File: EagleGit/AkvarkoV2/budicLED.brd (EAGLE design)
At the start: 114.3 x 160 mm, 59 parts, among them IC1 7805TV, Q1 BD243C, Q2 BD243C, Q3 BD243C, Q4 BD243C, T1 2N5551, T2 2N5551, T3 2N5551, T4 2N5551, U1 ARDUINOR3-DIMENSION, X1 SMKDSP_1,5/2, X2 SMKDSP_1,5/8, X3 SMKDSP_1,5/3

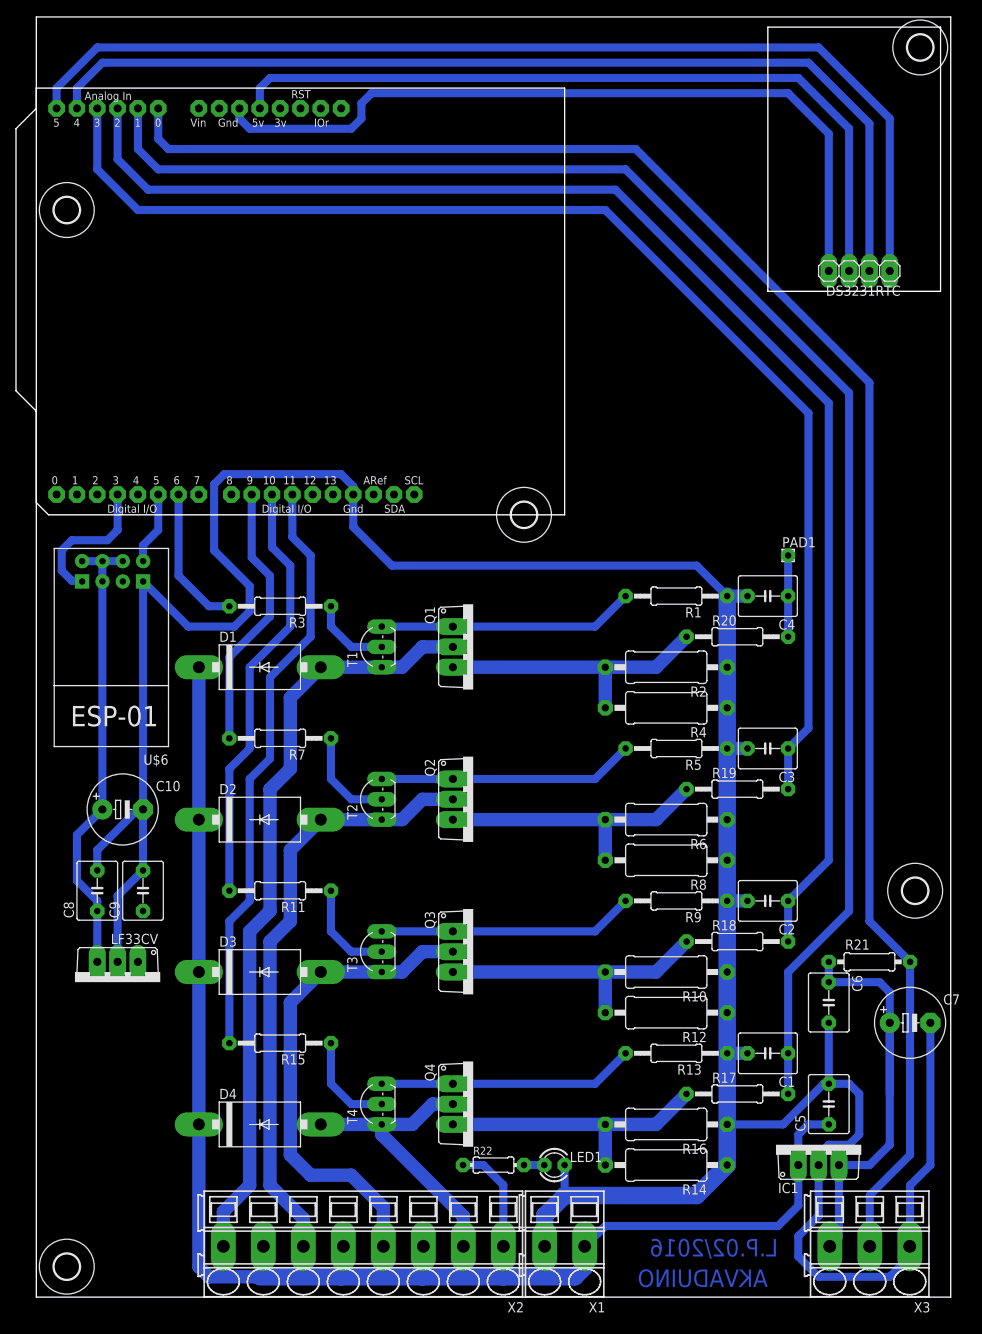
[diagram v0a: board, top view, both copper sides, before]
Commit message: Akvarko: - zakladni navrh DPS a rozmisteni soucastek.
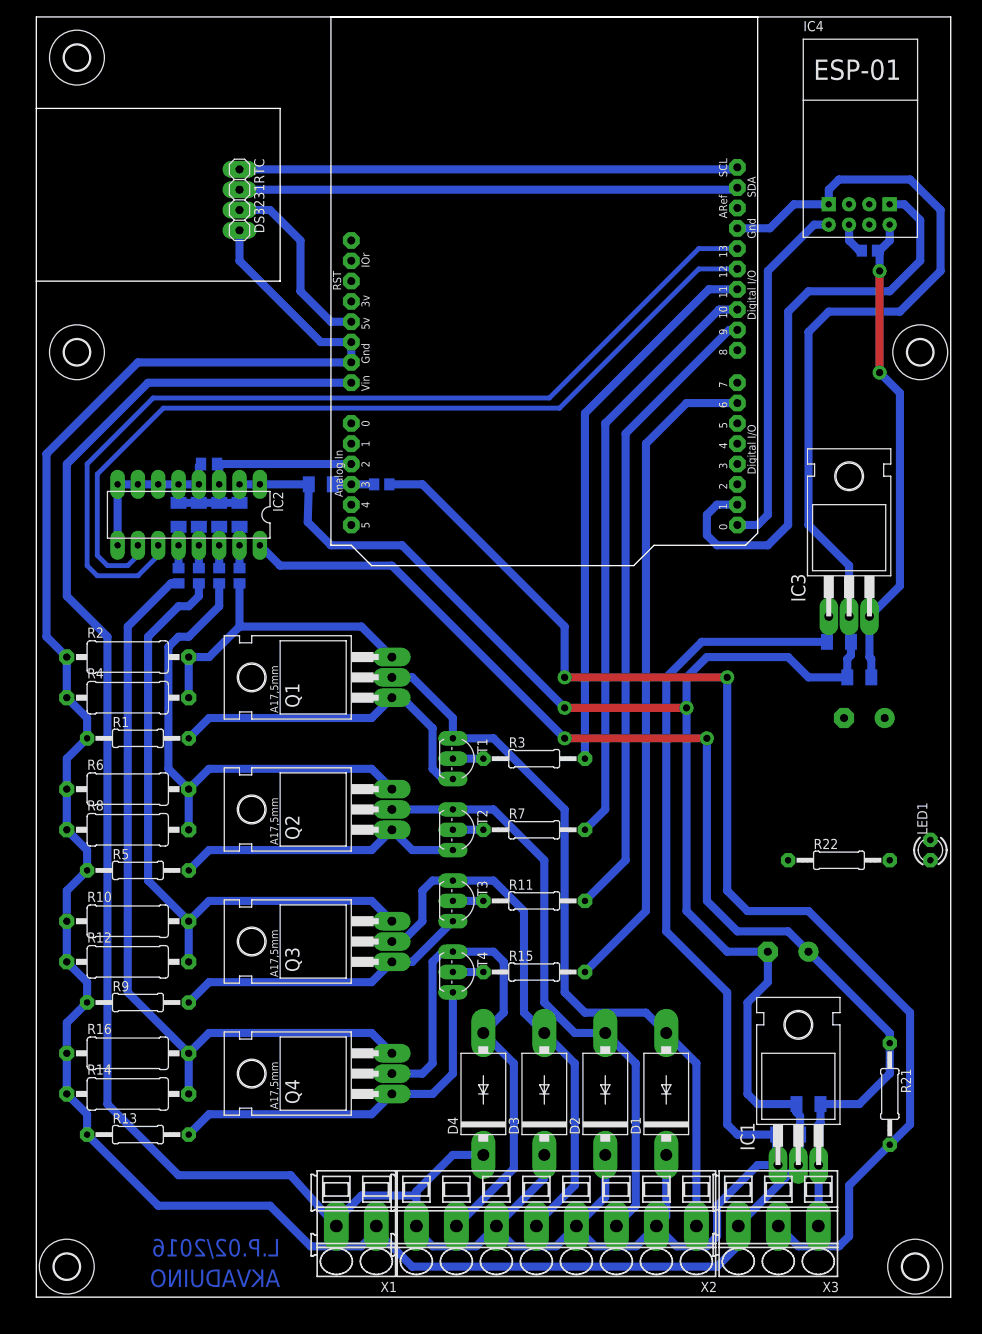
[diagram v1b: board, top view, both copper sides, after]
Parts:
- removed LF33CV: 7805TV, linear:TO220V
- removed PAD1: (no value), wirepad:1,6/0,8
- removed U$6: ESP01, esp8266modules:ESP01
- added C11: 330n, rcl:C0805K
- added C12: 330n, rcl:C1206K
- added IC2: 4051N, 40xx:DIL16
- added IC3: LF33CV, linear:TO220H
- added IC4: ESP01, esp8266modules:ESP01
- added R23, R24: 4k7, rcl:R0805
- C1, C2, C3, C4, C5, C6, C8, C9: device rcl:C050-050X075 -> rcl:C1206K
- C10, C7: device resistor:E5-8,5 -> resistor:E5-10,5
- IC1: value 7805TV -> 7805T; device linear:TO220V -> linear:TO220H
- Q1, Q2, Q3, Q4: device transistor:TO220V -> transistor:TO220
- R17, R18, R19, R20: device rcl:0207/12 -> rcl:R0805
- R21: device rcl:0207/10 -> rcl:0207/12
- R22: device rcl:0204/7 -> rcl:0207/12
- moved U$4 112.1 mm to (5.08, 118.1)
- moved C8 98.9 mm to (102.9, 77.5), flipped to the bottom, turned to 0 degrees
- moved C1 94.3 mm to (25.4, 97.8), flipped to the bottom, turned to 90 degrees
- moved C10 93.4 mm to (103.5, 72.4), flipped to the bottom
- moved C9 92.4 mm to (100.3, 81.9), flipped to the bottom, turned to 180 degrees
- moved R17 89.8 mm to (25.4, 90.2), flipped to the bottom, turned to 90 degrees
- moved C2 83.9 mm to (22.9, 97.8), flipped to the bottom, turned to 90 degrees
- moved R18 79.3 mm to (22.9, 90.2), flipped to the bottom, turned to 90 degrees
- moved DS3231RTC 78.0 mm to (25.4, 137.2), turned to 270 degrees
- moved C3 76.9 mm to (20.3, 97.8), flipped to the bottom, turned to 90 degrees
- moved C4 74.4 mm to (17.8, 97.8), flipped to the bottom, turned to 90 degrees
- moved D1 73.7 mm to (78.7, 25.4), turned to 90 degrees
- moved R19 72.4 mm to (20.3, 90.2), flipped to the bottom, turned to 90 degrees
- moved R20 70.3 mm to (17.8, 90.2), flipped to the bottom, turned to 90 degrees
- moved R1 69.6 mm to (12.7, 69.8), turned to 0 degrees
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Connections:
- removed net +5V: C9.1, DS3231RTC.3, LF33CV.1, U1.5V
- removed net GND1: U1.GND1
- removed net N$16: R15.2, U1.D11
- removed net N$26: DS3231RTC.4, U1.GND2
- removed net VIN: U1.VIN
- new net N$29: C1.1, IC2.15, R17.2
- new net N$30: C2.1, IC2.14, R18.2
- new net N$31: C3.1, IC2.13, R19.2
- new net N$32: IC2.10, U1.D12
- new net N$33: C4.1, IC2.12, R20.2
- new net N$34: R3.2, U1.D11
- new net N$35: R15.2, U1.D6
- net +12V: now also C9.1, IC3.1, U1.VIN, X1.2, X2.2, X2.4, X2.6, X2.8; no longer X1.1, X2.1, X2.3, X2.5, X2.7
- net +3V3: now also IC3.3, IC4.VCC, R23.1; no longer LF33CV.3, U$6.CH_PD, U$6.VCC
- net GND: now also C11.2, C12.2, DS3231RTC.4, IC2.1, IC2.2, IC2.4, IC2.5, IC2.6, IC2.7, IC2.8, IC2.9, IC3.2, IC4.GND, U1.GND1, U1.GND2, X1.1, X3.3; no longer LF33CV.2, U$6.GND, X1.2, X3.1
- net N$10: now also R21.2, R24.1, X3.2; no longer R3.2, U1.D6
- net N$13: now also U1.SCL; no longer U1.A5
- net N$15: now also U1.D9; no longer U1.D10
- net N$17: now also IC4.CH_PD, R23.2; no longer C4.1, PAD1.1, R20.2
- net N$18: now also C11.1, IC2.3; no longer C2.1, R18.2
- net N$19: now also DS3231RTC.3, U1.5V; no longer C3.1, R19.2, U1.A3
- net N$2: now also X2.1; no longer X2.8
- net N$20: now also IC2.11, U1.D13; no longer C1.1, R17.2, U1.A1
- net N$21: now also C12.1, R24.2, U1.A3; no longer R21.2, U1.A0, X3.2
- net N$22: now also U1.D10; no longer U1.D9
- net N$23: now also IC2.16, X3.1; no longer X3.3
- net N$24: now also U1.SDA; no longer U1.A4
- net N$25: now also IC4.TX, U1.D0; no longer U$6.TX, U1.D5
- net N$28: now also IC4.RX, U1.D1; no longer U$6.RX, U1.D3
- net N$4: now also X2.3; no longer X2.6
- net N$5: now also X2.5; no longer X2.4
- net N$7: now also X2.7; no longer X2.2
- net SENS1: now also R20.1; no longer R17.1
- net SENS2: now also R19.1; no longer R18.1
- net SENS3: now also R18.1; no longer R19.1
- net SENS4: now also R17.1; no longer R20.1
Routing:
- net N$21: track 217.5 -> 5.17 mm
- net GND: track 379.8 -> 570.7 mm, vias 0 -> 2
- net +12V: track 199.5 -> 369.2 mm
- net N$18: track 177.3 -> 19.4 mm
- net N$10: track 18.1 -> 153.3 mm, vias 0 -> 2
- net N$19: track 157.2 -> 23.5 mm
- net N$32: track 0.00 -> 108.2 mm
- net N$26: track 97.7 -> 0.00 mm
- net +5V: track 97.1 -> 0.00 mm
- net N$23: track 56.7 -> 146.6 mm, vias 0 -> 2
- net N$35: track 0.00 -> 82.7 mm
- net N$20: track 197.4 -> 116.9 mm
- net N$16: track 73.7 -> 0.00 mm
- net N$13: track 131.5 -> 62.3 mm
- net N$34: track 0.00 -> 68.6 mm
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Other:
- outline, holes or cut-outs redrawn

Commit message: Akvarko2: - navržené DPS. x bylo by vhodné doplnit filtrační kondenzátory k napájecím vstupům.
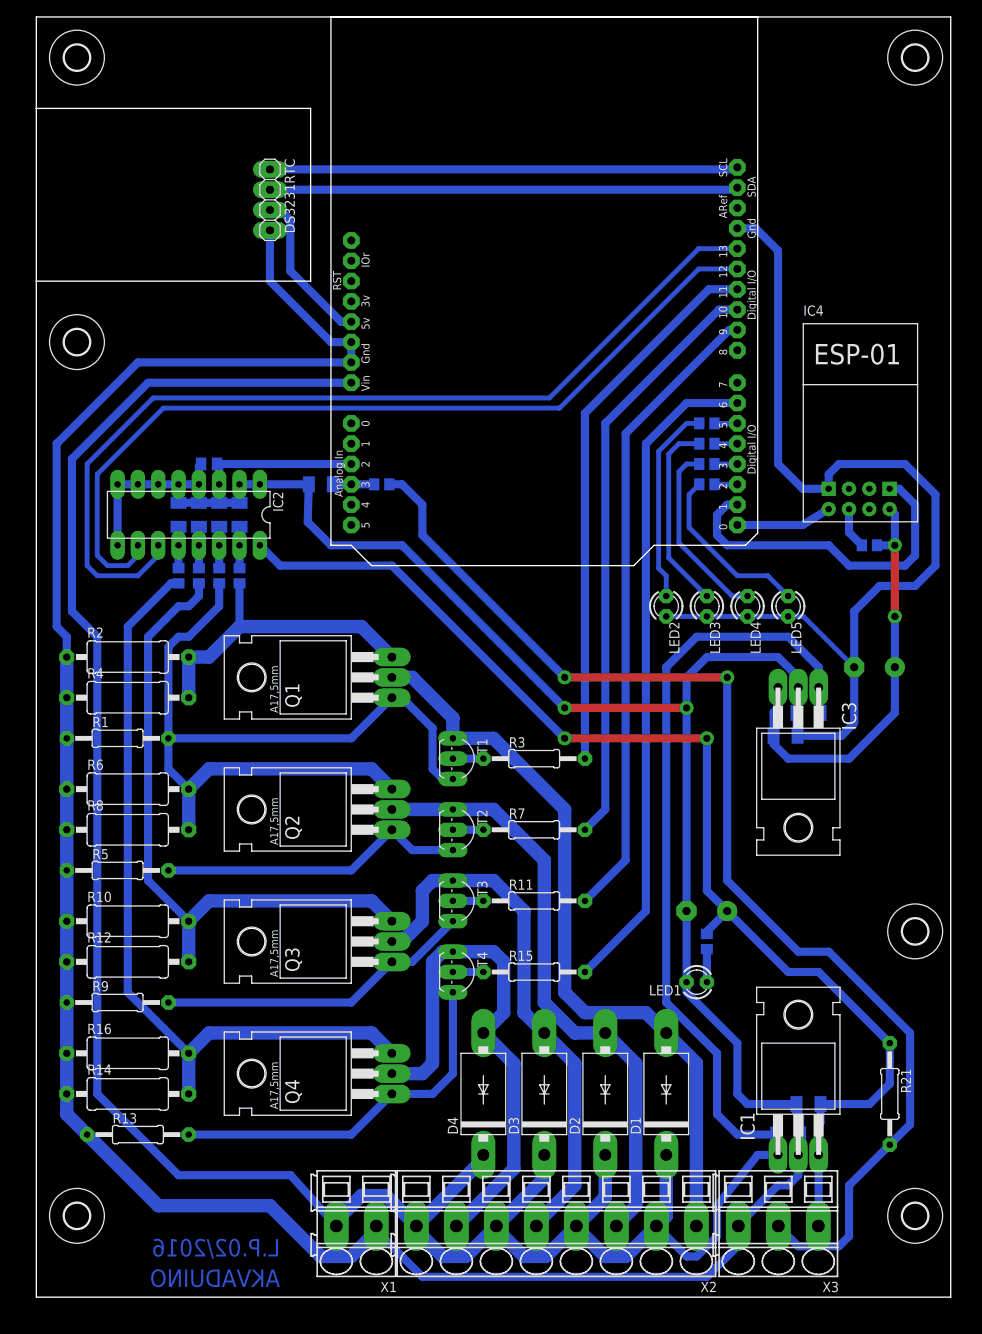
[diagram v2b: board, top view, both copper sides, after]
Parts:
- added LED2, LED3, LED4, LED5: 2.2V 5mA, led:LED3MM
- added R25, R26, R27, R28: 4k7, rcl:R0805
- added U$6: (no value), holes:3,2
- R22: device rcl:0207/12 -> rcl:R0805
- moved U$5 36.8 mm to (109.9, 154.9)
- moved R23 36.8 mm to (104.1, 94.0)
- moved IC4 35.6 mm to (102.9, 106.7)
- moved IC3 34.9 mm to (95.2, 63.5), turned to 180 degrees
- moved LED1 33.6 mm to (82.5, 39.4), turned to 180 degrees
- moved R22 19.4 mm to (83.8, 44.5), flipped to the bottom, turned to 270 degrees
- moved C8 11.8 mm to (93.7, 70.2), turned to 180 degrees
- moved C7 11.4 mm to (83.8, 48.3)
- moved C9 9.67 mm to (96.5, 73.0), turned to 0 degrees
- moved U$2 6.48 mm to (5.08, 10.2)
- moved C10 6.48 mm to (104.8, 78.7)
- moved U$3 6.35 mm to (109.9, 10.2)
- moved DS3231RTC 3.81 mm to (29.2, 137.2)
- moved R1 2.54 mm to (10.2, 69.8)
- moved R5 2.54 mm to (10.2, 53.3)
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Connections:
- new net N$16: R28.2, U1.D2
- new net N$26: R27.2, U1.D3
- new net N$36: R26.2, U1.D4
- new net N$37: R25.2, U1.D5
- new net N$38: LED5.A, R28.1
- new net N$39: LED4.A, R27.1
- new net N$40: LED3.A, R26.1
- new net N$41: LED2.A, R25.1
- net +12V: no longer R22.1
- net GND: now also LED2.K, LED3.K, LED4.K, LED5.K
- net N$23: now also R22.1
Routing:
- net N$25: track 44.8 -> 12.0 mm
- net N$28: track 74.2 -> 42.8 mm
- net N$41: track 0.00 -> 25.0 mm
- net N$40: track 0.00 -> 24.1 mm
- net N$39: track 0.00 -> 23.2 mm
- net N$38: track 0.00 -> 21.9 mm
- net GND: track 570.7 -> 582.9 mm
- net +3V3: track 60.3 -> 53.5 mm
- net N$27: track 0.00 -> 4.13 mm
- net N$19: track 23.5 -> 19.7 mm
- net N$24: track 62.5 -> 58.7 mm
- net N$13: track 62.3 -> 58.5 mm
- net N$10: track 153.3 -> 149.6 mm
- net +12V: track 369.2 -> 372.7 mm
- net N$23: track 146.6 -> 149.7 mm
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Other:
- outline, holes or cut-outs redrawn
